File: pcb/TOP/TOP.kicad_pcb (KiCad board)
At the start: 2 copper layers, 52 x 63 mm, 97 parts, among them J1 Conn_01x04, Q1 BF545A, Q2 BF545A, U1 ICL7660, U2 L78L15_SOT89, U3 TL074, U4 OPA2604

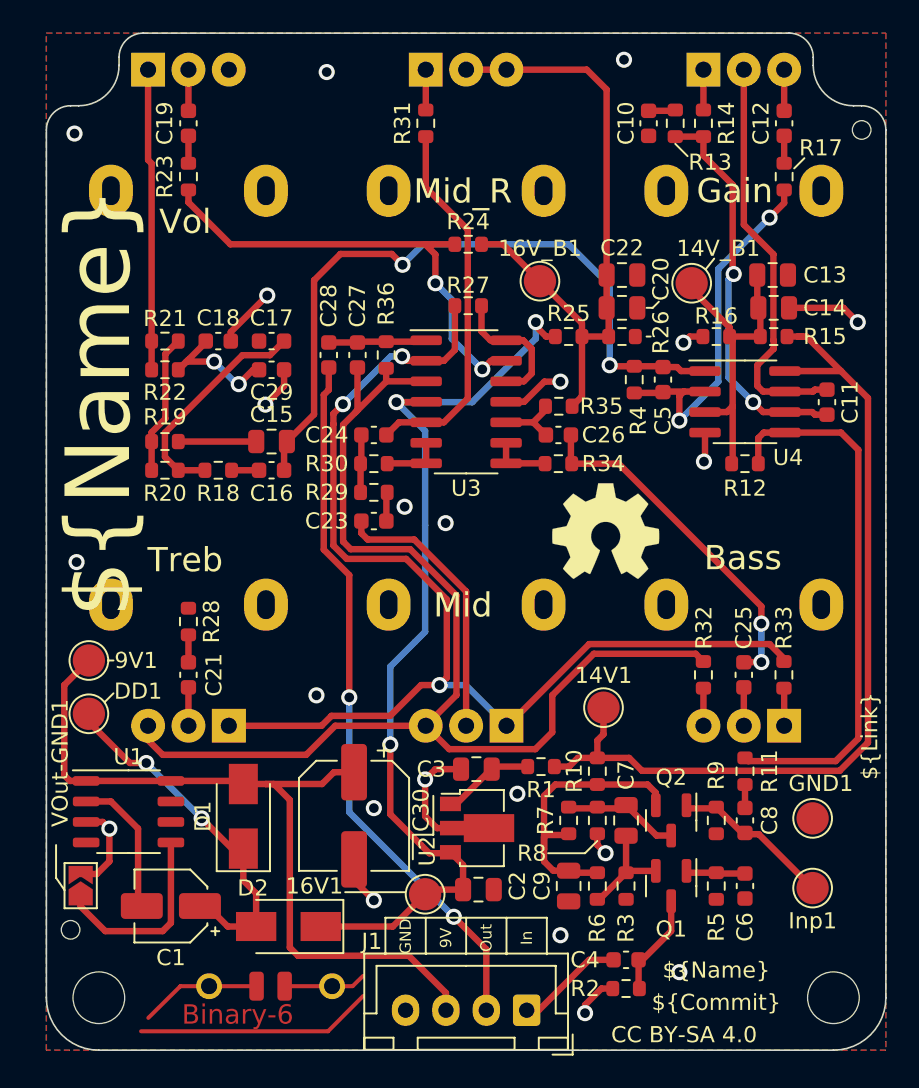
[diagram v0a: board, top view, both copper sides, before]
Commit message: [TOP] Fix various problems of first design:
- Some pins of TL072 swapped
- Volume pot inverted
- BOOST input of 7660 now only settable via jumper
- Add option of TO-92/BF245 instead of SOT-23/BF545
-
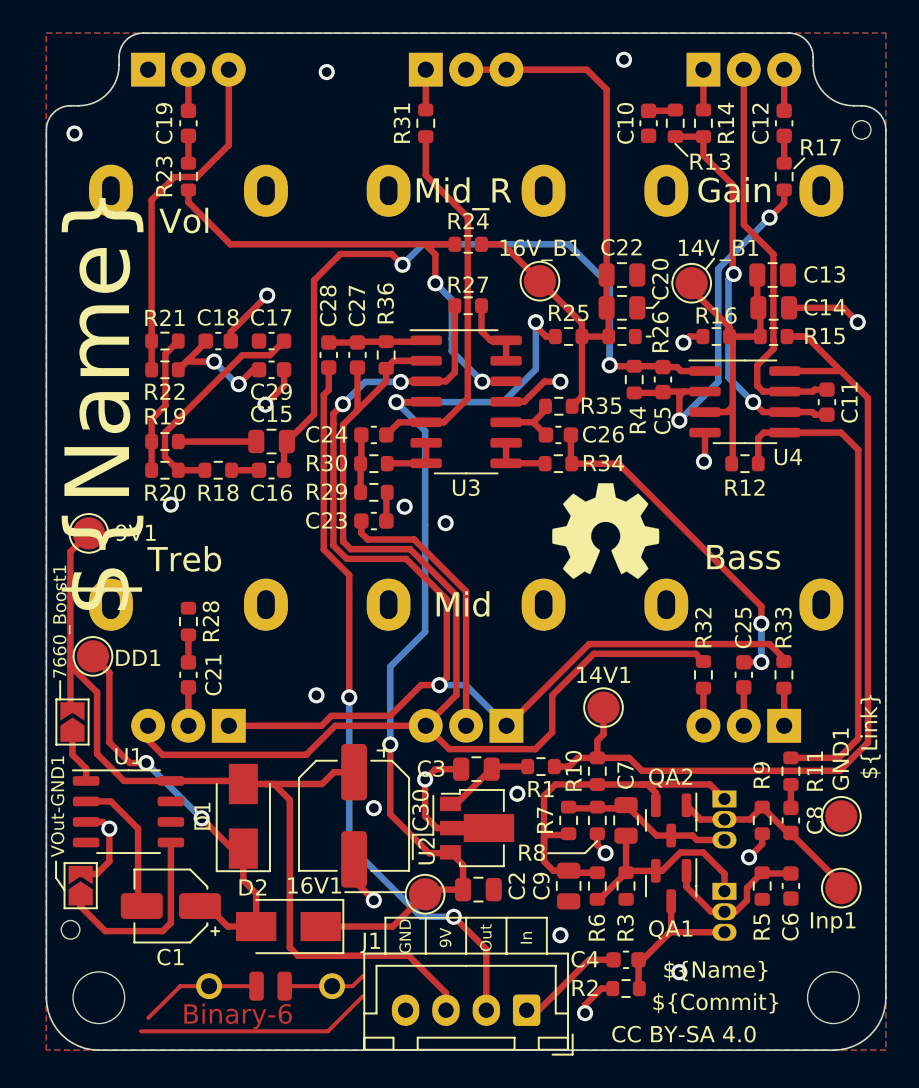
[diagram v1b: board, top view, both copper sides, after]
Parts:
- added 7660_Boost1: Jmp, Jumper:SolderJumper-2_P1.3mm_Open_TrianglePad1.0x1.5mm, F.Cu at (125.1, 110.2)
- added QB1: BF245A, Package_TO_SOT_THT:TO-92L_Inline, B.Cu at (165.5, 120.7)
- added QB2: BF245A, Package_TO_SOT_THT:TO-92L_Inline, B.Cu at (165.5, 114.9)
- moved 9V1 7.87 mm to (126.1, 98.5)
- moved DD1 3.57 mm to (126.4, 106.1)
- moved C6 2.84 mm to (169.6, 120.3)
- moved C8 2.84 mm to (169.6, 116.3)
- moved R11 2.84 mm to (169.6, 113.2)
- moved R5 2.84 mm to (167.8, 120.3)
- moved R9 2.84 mm to (167.8, 116.3)
- moved GND1 1.78 mm to (172.7, 116.0)
- moved Inp1 1.78 mm to (172.7, 120.5)
- renumbered Q1 to QA1, Q2 to QA2
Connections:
- R23 pad 2: Net-(U3-Pad13) -> Net-(R23-Pad2)
- R24 pad 2: Net-(U3-Pad13) -> Net-(R23-Pad2)
- R27 pad 2: Net-(U3-Pad2) -> Net-(R27-Pad2)
- R33 pad 2: Net-(U3-Pad2) -> Net-(R27-Pad2)
- RV3 pad 1: Net-(R21-Pad2) -> GND
- RV3 pad 3: GND -> Net-(R21-Pad2)
- RV5 pad 1: Net-(U3-Pad2) -> Net-(R27-Pad2)
- RV6 pad 1: Net-(U3-Pad2) -> Net-(R27-Pad2)
- U1 pad 1: +9V -> Net-(U1-Pad1)
- U3 pad 12: Net-(R27-Pad1) -> Net-(R23-Pad2)
- U3 pad 13: Net-(U3-Pad13) -> Net-(R27-Pad1)
- U3 pad 2: Net-(U3-Pad2) -> Net-(C27-Pad2)
- U3 pad 3: Net-(C27-Pad2) -> Net-(R27-Pad2)
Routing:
- net Net-(R27-Pad2): track 0.00 -> 73.9 mm, vias 0 -> 3
- net Net-(U3-Pad2): track 73.3 -> 0.00 mm, vias 3 -> 0
- net Net-(R23-Pad2): track 0.00 -> 29.8 mm, vias 0 -> 2
- net Net-(U3-Pad13): track 29.3 -> 0.00 mm, vias 2 -> 0
- net +9V: track 49.2 -> 57.6 mm
- net Net-(C7-Pad2): track 6.64 -> 13.0 mm
- net Net-(C6-Pad1): track 3.69 -> 9.74 mm
- net Net-(C9-Pad1): track 18.3 -> 23.8 mm
- net Net-(R27-Pad1): track 8.46 -> 4.61 mm
- net Net-(C4-Pad1): track 6.41 -> 10.0 mm
- net Net-(C1-Pad1): track 22.5 -> 26.0 mm
- net Net-(C7-Pad1): track 7.18 -> 10.6 mm
- net Net-(U1-Pad1): track 0.00 -> 3.28 mm
- net Net-(R11-Pad2): track 33.9 -> 30.9 mm
- net Net-(R21-Pad2): track 18.7 -> 21.4 mm
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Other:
- board text added: "D"
- board text added: "G"
- board text added: "S"

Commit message: [TOP] Silk beautification
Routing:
- net GND: track 39.6 -> 40.9 mm
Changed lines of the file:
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@@
     (property "Sheetname" "")
     (attr smd)
-    (fp_text reference "C3" (at 2.794 0) (layer "F.SilkS")
+    (fp_text reference "C3" (at 2.794 0.508) (layer "F.SilkS")
       (effects (font (size 1 1) (thickness 0.15)))
     )
@@
     (property "Sheetname" "")
     (attr smd)
-    (fp_text reference "D1" (at 0 -2.5 90) (layer "F.SilkS")
+    (fp_text reference "D1" (at -1.651 -2.5 90) (layer "F.SilkS")
       (effects (font (size 1 1) (thickness 0.15)))
     )
@@
   (segment (start 167.839 117.093) (end 167.839 117.741) (width 0.4) (layer "F.Cu") (net 2))
   (segment (start 126.624 119.586) (end 127.402 118.808) (width 0.4) (layer "F.Cu") (net 2))
-  (segment (start 138.223164 89.358644) (end 137.067164 90.514644) (width 0.4) (layer "F.Cu") (net 2))
-  (segment (start 138.223164 88.355644) (end 138.223164 89.358644) (width 0.4) (layer "F.Cu") (net 2))
   (segment (start 134.921164 86.015836) (end 134.921164 86.577644) (width 0.4) (layer "F.Cu") (net 2))
   (segment (start 137.181 83.756) (end 134.921164 86.015836) (width 0.4) (layer "F.Cu") (net 2))
@@
   (segment (start 164.297 92.244) (end 164.297 93.978) (width 0.4) (layer "F.Cu") (net 2))
   (segment (start 127.402 118.808) (end 127.402 116.776) (width 0.4) (layer "F.Cu") (net 2))
+  (segment (start 135.583808 90.995) (end 138.223164 88.355644) (width 0.4) (layer "F.Cu") (net 2))
+  (segment (start 135.403 90.995) (end 135.583808 90.995) (width 0.4) (layer "F.Cu") (net 2))
   (segment (start 157.628 117.789914) (end 158.137043 118.298957) (width 0.4) (layer "F.Cu") (net 2))
   (segment (start 167.839 117.741) (end 167.026 118.554) (width 0.4) (layer "F.Cu") (net 2))
@@
   (via (at 125.243 73.723) (size 1) (drill 0.6) (layers "F.Cu" "B.Cu") (free) (net 2))
   (via (at 162.708 125.666) (size 1) (drill 0.6) (layers "F.Cu" "B.Cu") (free) (net 2))
-  (via (at 131.212 96.71) (size 1) (drill 0.6) (layers "F.Cu" "B.Cu") (free) (net 2))
+  (via (at 131.212 97.472) (size 1) (drill 0.6) (layers "F.Cu" "B.Cu") (free) (net 2))
   (via (at 145.69 96.837) (size 1) (drill 0.6) (layers "F.Cu" "B.Cu") (free) (net 2))
   (via (at 152.675 114.617) (size 1) (drill 0.6) (layers "F.Cu" "B.Cu") (free) (net 2))
@@
   (via (at 137.181 83.756) (size 1) (drill 0.6) (layers "F.Cu" "B.Cu") (net 2))
   (via (at 159.279 69.151) (size 1) (drill 0.6) (layers "F.Cu" "B.Cu") (free) (net 2))
-  (via (at 137.067164 90.514644) (size 1) (drill 0.6) (layers "F.Cu" "B.Cu") (net 2))
+  (via (at 135.403 90.995) (size 1) (drill 0.6) (layers "F.Cu" "B.Cu") (net 2))
   (via (at 148.23 97.853) (size 1) (drill 0.6) (layers "F.Cu" "B.Cu") (free) (net 2))
   (segment (start 153.25 128.025) (end 153.999 128.025) (width 0.4) (layer "F.Cu") (net 3))
